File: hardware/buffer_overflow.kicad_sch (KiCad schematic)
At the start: 19 parts, among them J2 E1, U1 LM741

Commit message: Some updates based on feedback from freestompboxes.org folks:
 - Add back thermal reliefs on ground pads
 - Switch to stereo jacks for improved mechanical support
 - Add 3D models for various parts (courtesy of Vasily Kashirin - https://grabcad.com/vasily.kashirin-1/models?page=1)
 - Add more space between potentiometers (need to update the courtyard to make this more obvious in the future)
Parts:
- J2: footprint Connector_Molex:Molex_PicoBlade_53047-0410_1x04_P1.25mm_Vertical -> buffer_overflow:Molex_PicoBlade_53047-0410_1x04_P1.25mm_Vertical_with_3D_Model
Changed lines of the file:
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@@
   (title_block
     (title "Buffer Overflow Drive Effect")
-    (date "2023-03-03")
-    (rev "v0.38")
+    (date "2023-03-04")
+    (rev "v0.39")
     (company "github.com/whbeers/buffer_overflow")
   )
@@
       (effects (font (size 1.27 1.27)) (justify left))
     )
-    (property "Footprint" "Connector_Molex:Molex_PicoBlade_53047-0410_1x04_P1.25mm_Vertical" (at 111.76 106.68 0)
-      (effects (font (size 1.27 1.27)) hide)
-    )
+    (property "Footprint" "buffer_overflow:Molex_PicoBlade_53047-0410_1x04_P1.25mm_Vertical_with_3D_Model" (at 111.76 106.68 0)
+      (effects (font (size 1.27 1.27)) hide)
+    )

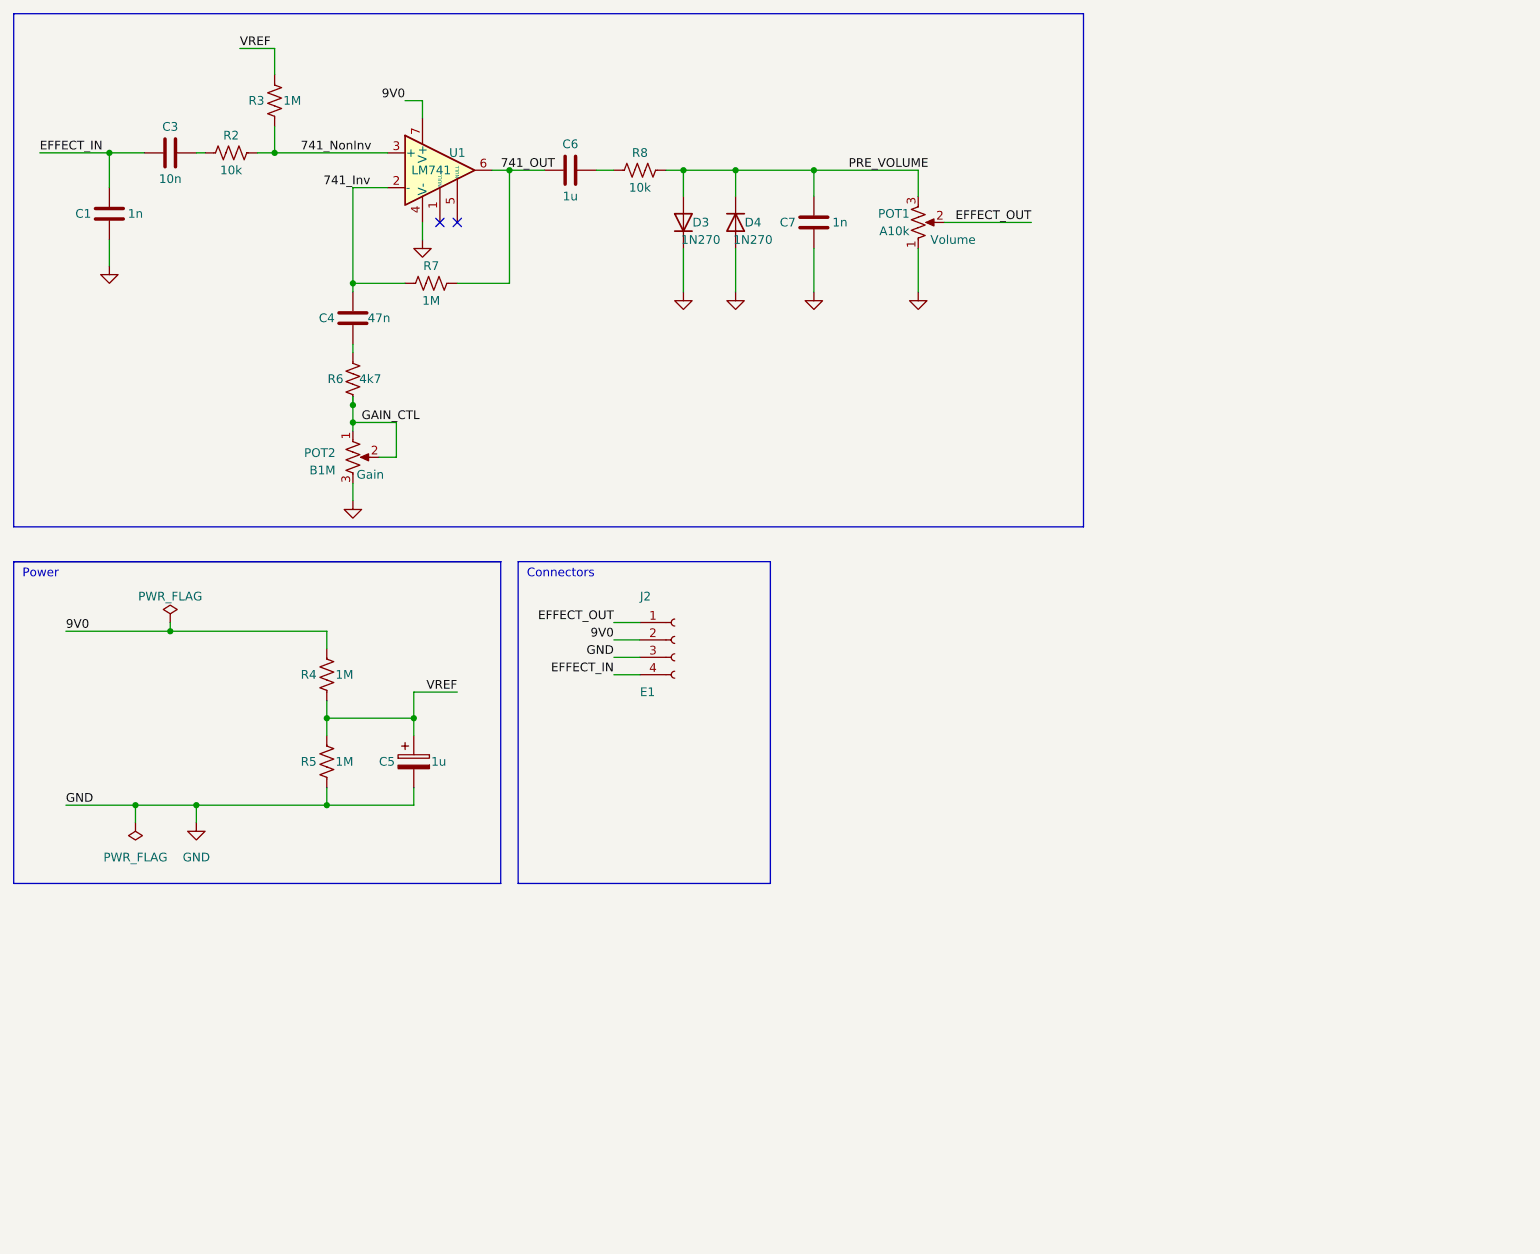
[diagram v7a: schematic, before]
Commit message: v0.40 - proof-of-concept for Noise Floor UX board
 - change to SMD resistors and capacitors
 - full re-layout and re-route to accomodate board-to-board assemblies
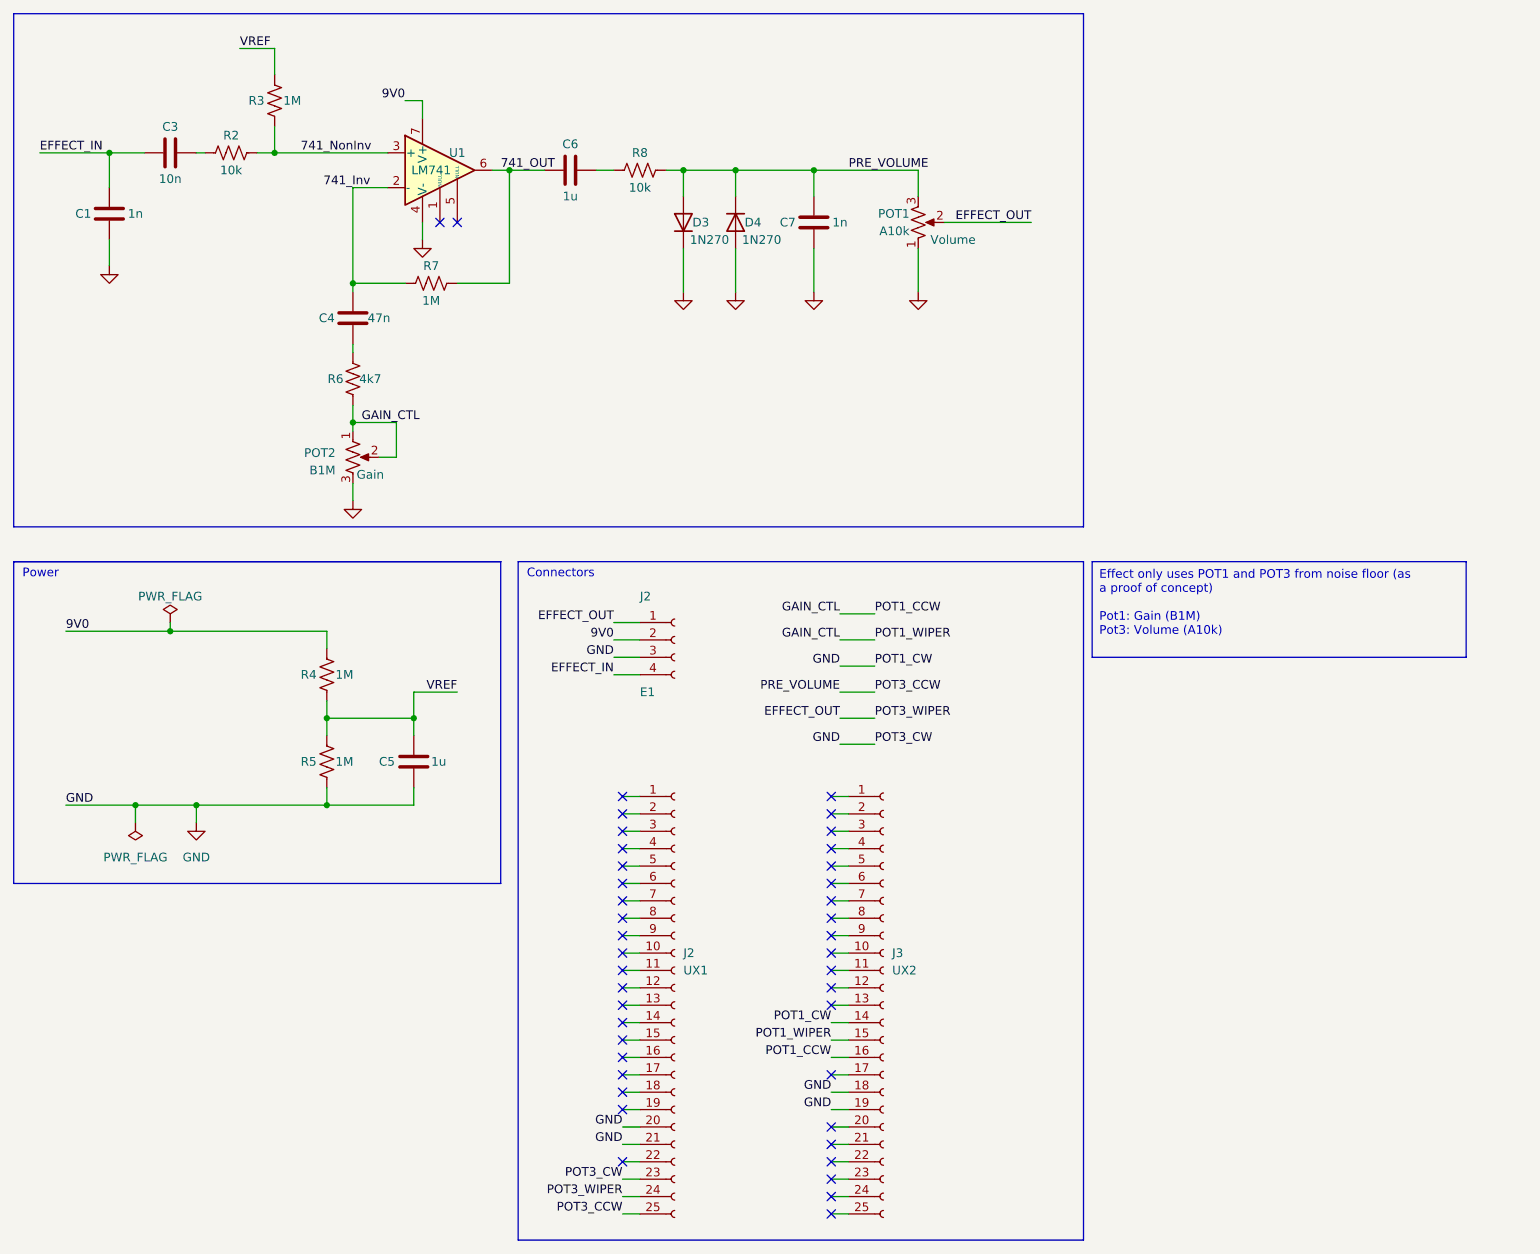
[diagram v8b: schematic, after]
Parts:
- added J2: UX1, buffer_overflow:Amphenol_Header_25Pin_10162582-1134125LF, symbol Connector:Conn_01x25_Socket
- added J3: UX2, buffer_overflow:Amphenol_Header_25Pin_10162582-1134125LF, symbol Connector:Conn_01x25_Socket
- C1, C3, C4, C7: footprint Capacitor_THT:C_Rect_L7.2mm_W2.5mm_P5.00mm_FKS2_FKP2_MKS2_MKP2 -> Capacitor_SMD:C_1206_3216Metric_Pad1.33x1.80mm_HandSolder
- C5: footprint Capacitor_THT:CP_Radial_D5.0mm_P2.50mm -> Capacitor_SMD:C_1206_3216Metric_Pad1.33x1.80mm_HandSolder; symbol Device:C_Polarized -> Device:C
- C6: footprint Capacitor_THT:C_Rect_L7.2mm_W5.5mm_P5.00mm_FKS2_FKP2_MKS2_MKP2 -> Capacitor_SMD:C_1206_3216Metric_Pad1.33x1.80mm_HandSolder
- POT1, POT2: footprint buffer_overflow:Potentiometer_Single_3_Horizontal -> (none)
- R2, R3, R4, R5, R6, R7, R8: footprint Resistor_THT:R_Axial_DIN0207_L6.3mm_D2.5mm_P7.62mm_Horizontal -> Resistor_SMD:R_1206_3216Metric_Pad1.30x1.75mm_HandSolder
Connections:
- net EFFECT_OUT: now also J2.24 (Pin_24)
- net GAIN_CTL: now also J3.15 (Pin_15), J3.16 (Pin_16)
- net GND: now also J2.20 (Pin_20), J2.21 (Pin_21), J2.23 (Pin_23), J3.14 (Pin_14), J3.18 (Pin_18), J3.19 (Pin_19)
- net PRE_VOLUME renamed POT3_CCW
- net POT3_CCW: now also J2.25 (Pin_25)
- no-connect marks 2 -> 42
